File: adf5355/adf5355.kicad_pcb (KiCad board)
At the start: 2 copper layers, 48.3 x 48.3 mm, 86 parts, among them J1 REF_IN_A, J2 RF_B, J3 RF_A_P, J4 REF_IN_B, J5 RF_A_N, J6 Conn_01x02_Male, J7 Conn_01x10_Male, U1 L7806, U2 ADM7150, U3 ADM7150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

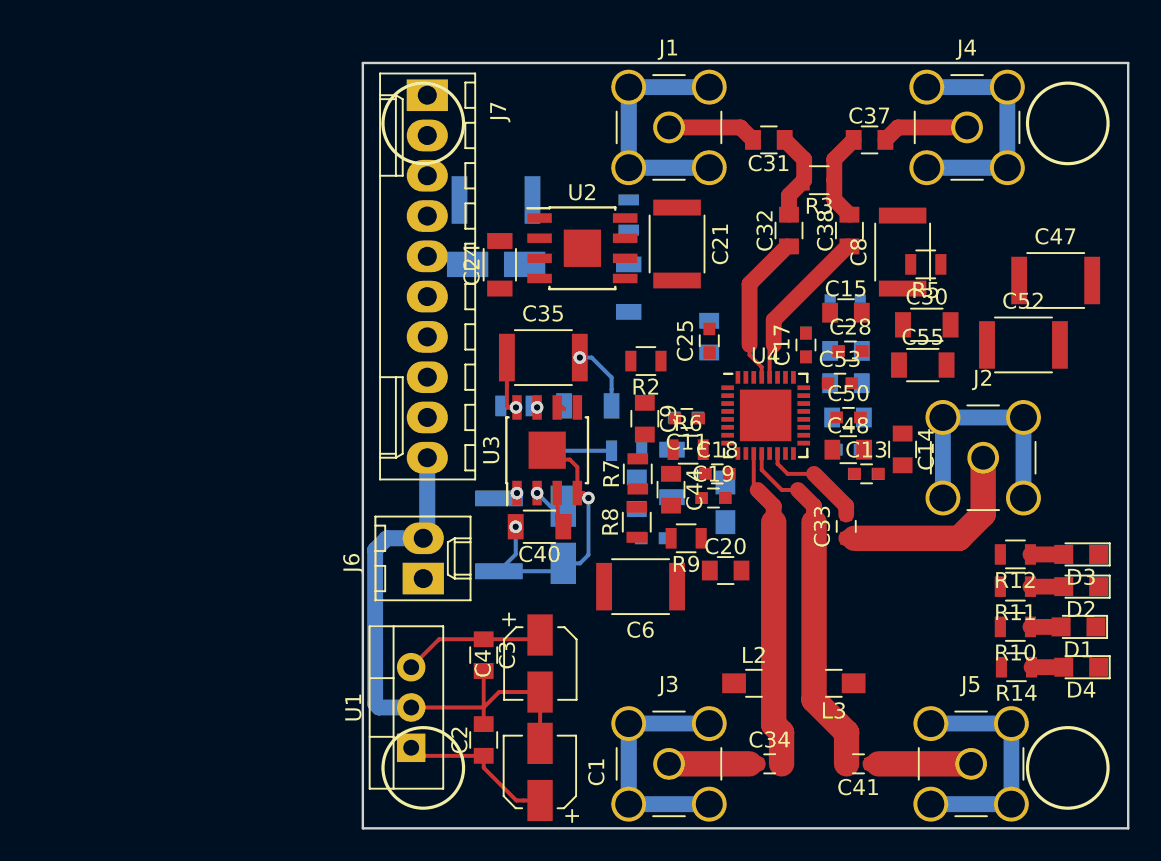
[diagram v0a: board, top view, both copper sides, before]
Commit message: Placing more components
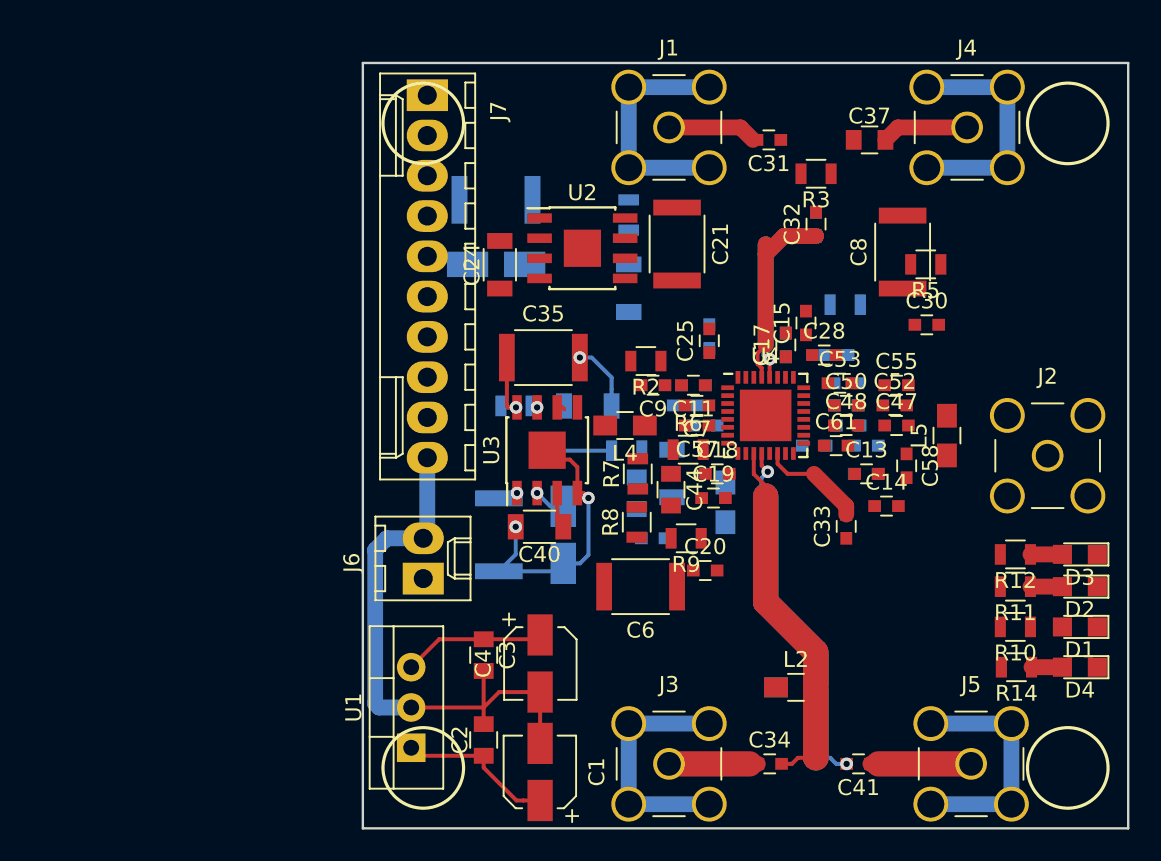
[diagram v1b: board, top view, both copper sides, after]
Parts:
- added C5: 1u, Capacitors_SMD:C_0603, B.Cu at (104.1, 100.3)
- added C56: 100p, Capacitors_SMD:C_0603, B.Cu at (105.4, 101.6)
- added C57: 10p, Capacitors_SMD:C_0603, F.Cu at (104.9, 101.6)
- added C58: 1u, Capacitors_SMD:C_0603, F.Cu at (118.1, 104.1)
- added C59: 10n, Capacitors_SMD:C_0603, B.Cu at (115.6, 102.9)
- added C60: 100p, Capacitors_SMD:C_0603, B.Cu at (112.3, 102.9)
- added C61: 10p, Capacitors_SMD:C_0603, F.Cu at (113.7, 102.9)
- added C7: 10n, Capacitors_SMD:C_0603, F.Cu at (104.9, 100.3)
- added L4: L, Capacitors_SMD:C_0805_HandSoldering, F.Cu at (100.3, 101.6)
- added L5: L, Capacitors_SMD:C_0805_HandSoldering, F.Cu at (120.7, 102.2)
- C14, C15, C20, C26, C29, C31, C32, C48, C51, C54, C9: footprint Capacitors_SMD:C_0805 -> Capacitors_SMD:C_0603
- C30, C55: footprint Capacitors_SMD:C_1206 -> Capacitors_SMD:C_0603
- C38: footprint Capacitors_SMD:C_0805 -> Capacitors_SMD:C_0603; moved to B.Cu
- C47, C52: footprint Capacitors_SMD:C_1812 -> Capacitors_SMD:C_0603
- L3: moved to B.Cu
- moved C47 13.6 mm to (117.5, 101.6)
- moved C52 8.97 mm to (117.4, 100.3)
- moved J2 4.07 mm to (127.0, 103.5)
- moved C14 3.71 mm to (116.8, 106.7), turned to 0 degrees
- moved L2 2.66 mm to (111.1, 118.1)
- moved C15 2.61 mm to (111.8, 95.1), turned to 90 degrees
- moved L3 2.41 mm to (111.1, 118.1), turned to 0 degrees
- moved C9 2.17 mm to (102.1, 99.1), turned to 180 degrees
- moved C38 2.15 mm to (112.4, 88.9)
- moved C11 2.14 mm to (104.7, 99.1)
- moved C55 2.08 mm to (117.5, 99.1)
- moved C10 2.08 mm to (104.7, 99.1)
- moved C32 1.75 mm to (112.4, 88.9)
- moved C28 1.67 mm to (112.9, 97.2)
- moved C48 1.53 mm to (114.3, 101.6)
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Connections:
- U2 pad 5: Net-(U2-Pad5) -> Net-(C23-Pad1)
- U3 pad 5: Net-(U3-Pad5) -> Net-(C39-Pad1)
- U4 pad 17: /5V -> Net-(C58-Pad1)
- U4 pad 6: /5V -> Net-(C5-Pad1)
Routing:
- net GND: track 137.1 -> 121.8 mm
- net Net-(C33-Pad1): track 12.8 -> 0.00 mm
- net Net-(C37-Pad1): track 5.62 -> 0.00 mm
- net Net-(C31-Pad1): track 5.62 -> 0.00 mm
- net Net-(C32-Pad1): track 9.68 -> 12.4 mm
- net Net-(C34-Pad2): track 20.8 -> 23.1 mm
- net Net-(D1-Pad2): track 1.93 -> 0.00 mm
- net Net-(C38-Pad1): track 10.4 -> 12.3 mm, vias 0 -> 1
- net Net-(C41-Pad2): track 22.9 -> 23.0 mm, vias 0 -> 2

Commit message: More layout placement
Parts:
- C5: moved to F.Cu
- moved C39 19.0 mm to (79.2, 97.5)
- moved C35 17.8 mm to (77.4, 97.3)
- moved C36 17.8 mm to (78.7, 108.5)
- moved C40 17.8 mm to (77.2, 108.0)
- moved R4 17.8 mm to (75.7, 100.4)
- moved U3 17.8 mm to (77.7, 103.2)
- moved C42 17.7 mm to (74.7, 108.5)
- moved R2 17.1 mm to (84.9, 101.1)
- moved C5 3.78 mm to (100.6, 101.6)
- moved C14 3.35 mm to (113.5, 106.2)
- moved C33 3.05 mm to (111.3, 108.0)
- moved C55 3.03 mm to (115.8, 96.5)
- moved L5 3.00 mm to (118.9, 104.6), turned to 0 degrees
- moved C12 2.78 mm to (112.8, 104.6)
- moved C7 2.74 mm to (102.6, 101.9), turned to 270 degrees
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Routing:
- net GND: track 121.8 -> 114.3 mm
- net Net-(C33-Pad2): track 6.62 -> 2.19 mm
- net Net-(C38-Pad1): track 12.3 -> 11.5 mm
- net Net-(C32-Pad1): track 12.4 -> 11.6 mm

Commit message: More placing
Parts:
- C43: footprint Capacitors_SMD:C_1206 -> Capacitors_SMD:C_0603; moved to F.Cu
- C44: footprint Capacitors_SMD:C_0805 -> Capacitors_SMD:C_0603
- C45: footprint Capacitors_SMD:C_0805 -> Capacitors_SMD:C_0603; moved to F.Cu
- C46: moved to F.Cu
- C47: footprint Capacitors_SMD:C_0603 -> Capacitors_SMD:C_1812
- R13: footprint Resistors_SMD:R_0805 -> Resistors_SMD:R_0603; moved to F.Cu
- R6, R7, R8, R9: footprint Resistors_SMD:R_0805 -> Resistors_SMD:R_0603
- moved C21 26.7 mm to (77.2, 86.1)
- moved U2 26.7 mm to (71.2, 86.4)
- moved C23 26.7 mm to (74.2, 88.9)
- moved C24 26.7 mm to (66.0, 87.4)
- moved R1 26.7 mm to (74.2, 84.3)
- moved C27 26.3 mm to (66.0, 84.8)
- moved C22 26.2 mm to (66.0, 91.9)
- moved C18 8.64 mm to (105.9, 114.3)
- moved R5 8.13 mm to (120.4, 99.5), turned to 90 degrees
- moved C19 5.34 mm to (106.2, 112.5)
- moved R13 5.00 mm to (105.0, 105.4), turned to 180 degrees
- moved R9 4.87 mm to (107.1, 105.3), turned to 270 degrees
- moved C30 3.57 mm to (115.8, 95.0)
- moved C46 3.48 mm to (105.4, 107.6), turned to 270 degrees
- moved C44 2.52 mm to (101.9, 104.6)
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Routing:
- net /3V3: track 0.00 -> 11.8 mm, vias 0 -> 2
- net Net-(R5-Pad1): track 0.00 -> 8.87 mm
- net Net-(R9-Pad1): track 0.00 -> 8.39 mm, vias 0 -> 1
- net Net-(C5-Pad1): track 0.00 -> 6.47 mm, vias 0 -> 1
- net Net-(C37-Pad1): track 0.00 -> 5.61 mm, vias 0 -> 1
- net Net-(C31-Pad1): track 0.00 -> 5.48 mm
- net Net-(C53-Pad1): track 0.00 -> 4.57 mm, vias 0 -> 1
- net Net-(C50-Pad1): track 0.00 -> 4.52 mm
- net GND: track 114.3 -> 116.4 mm, vias 3 -> 13
- net Net-(D1-Pad2): track 0.00 -> 2.01 mm
- net Net-(C25-Pad1): track 0.00 -> 1.65 mm, vias 0 -> 1
- net Net-(C58-Pad1): track 0.00 -> 0.81 mm
- added copper zone on B.Cu, net GND

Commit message: Started routing
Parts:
- L1: moved to F.Cu
- moved C18 4.38 mm to (106.7, 110.0), turned to 180 degrees
- moved C47 2.71 mm to (120.1, 102.1)
- moved C45 2.13 mm to (96.9, 106.8)
- moved R8 2.13 mm to (101.2, 107.6)
- moved R9 2.13 mm to (105.0, 105.9)
- moved C43 2.13 mm to (101.1, 105.3)
- moved C44 2.13 mm to (99.8, 105.3)
- moved R13 2.13 mm to (103.0, 106.0)
- moved C46 2.13 mm to (103.4, 108.2)
- moved R6 2.13 mm to (103.0, 104.6)
- moved R7 2.13 mm to (98.4, 106.9)
- moved C33 2.05 mm to (111.0, 105.9)
- moved C20 1.37 mm to (106.7, 111.3), turned to 180 degrees
- moved L1 1.27 mm to (107.4, 106.9)
- moved C19 0.51 mm to (106.7, 112.5), turned to 180 degrees
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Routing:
- net GND: track 116.4 -> 311.7 mm, vias 13 -> 50
- net Net-(C33-Pad1): track 0.00 -> 18.0 mm
- net /5V: track 2.05 -> 19.1 mm, vias 1 -> 3
- net /3V3: track 11.8 -> 22.8 mm
- net Net-(C28-Pad1): track 0.35 -> 5.65 mm, vias 0 -> 2
- net Net-(C43-Pad1): track 0.00 -> 4.72 mm
- net Net-(R6-Pad2): track 0.00 -> 4.52 mm
- net Net-(C45-Pad1): track 0.00 -> 3.69 mm
- net Net-(C46-Pad1): track 0.00 -> 3.43 mm
- net Net-(C58-Pad1): track 0.81 -> 3.82 mm, vias 0 -> 2
- net Net-(R9-Pad1): track 8.39 -> 10.0 mm, vias 1 -> 2
- net Net-(C43-Pad2): track 0.00 -> 1.16 mm
- net Net-(C50-Pad1): track 4.52 -> 5.12 mm, vias 0 -> 1
- added copper zone on In2.Cu, net /5V
- added copper zone on In1.Cu, net GND
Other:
- copper layers 2 -> 4

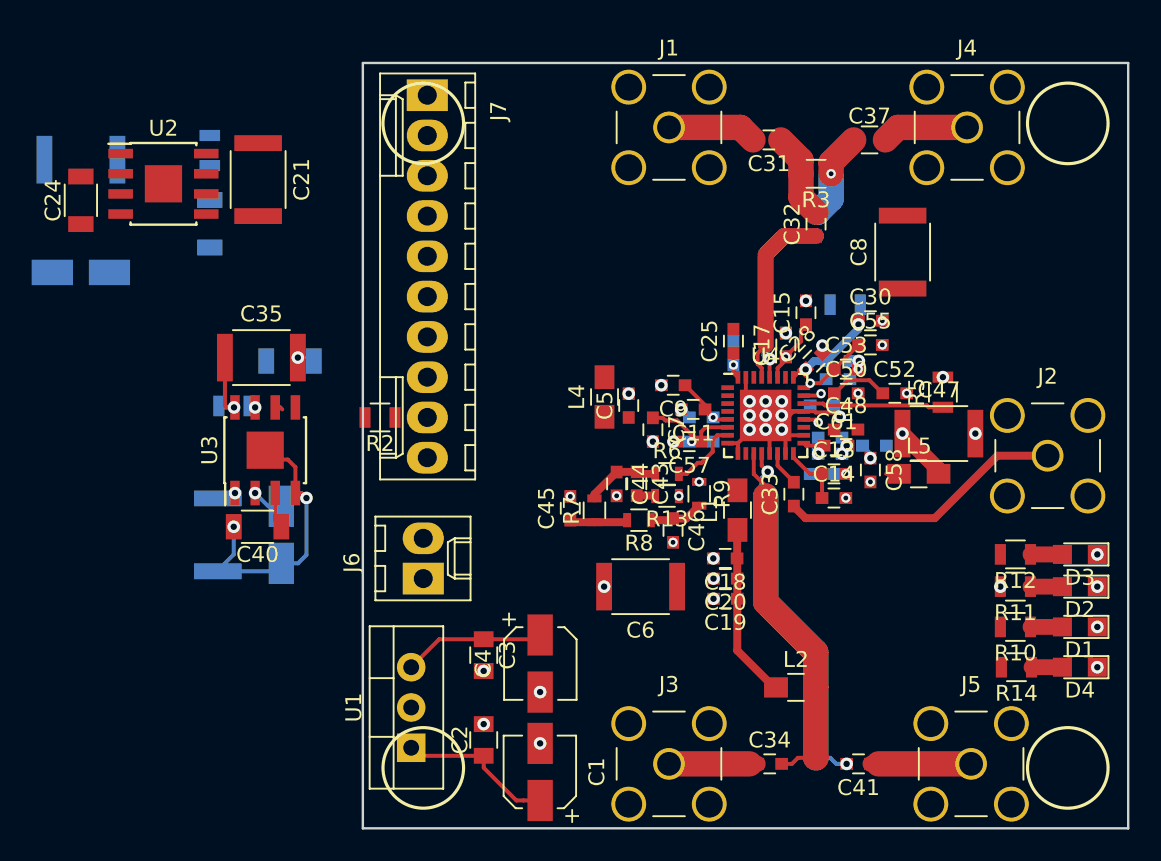
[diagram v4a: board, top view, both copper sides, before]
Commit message: Placement of LDOs and components
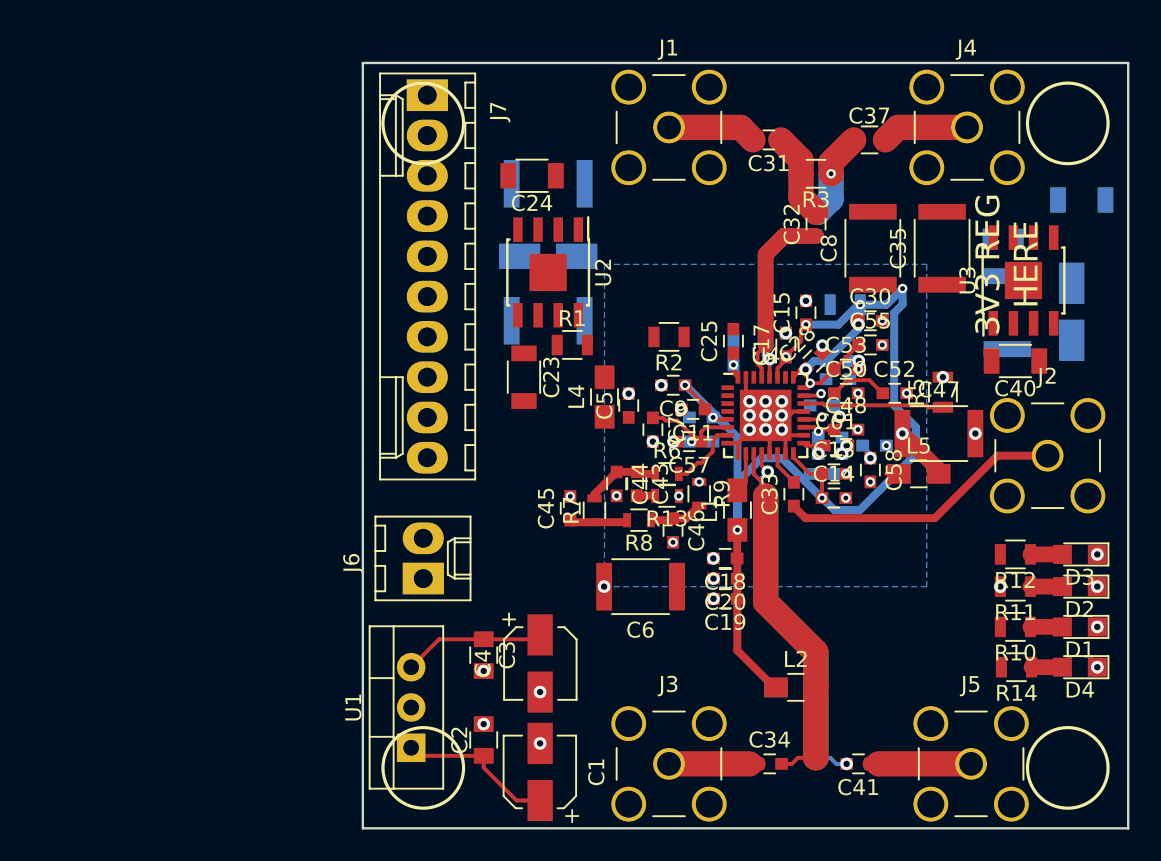
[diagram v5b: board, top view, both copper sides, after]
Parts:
- C21: moved to B.Cu
- C23, R1: moved to F.Cu
- moved C36 51.8 mm to (128.5, 94.4)
- moved C42 51.7 mm to (124.5, 94.5)
- moved C39 50.9 mm to (129.1, 87.4)
- moved R4 49.6 mm to (124.2, 89.8)
- moved U3 49.0 mm to (125.5, 92.5)
- moved C40 48.9 mm to (125.0, 97.5)
- moved C35 43.5 mm to (120.3, 90.4), turned to 90 degrees
- moved C27 29.5 mm to (95.5, 86.4)
- moved C22 29.5 mm to (95.5, 90.9)
- moved C24 28.5 mm to (94.5, 85.9), turned to 180 degrees
- moved R1 25.9 mm to (97.0, 96.5), turned to 0 degrees
- moved U2 24.9 mm to (95.5, 91.9), turned to 270 degrees
- moved C23 22.0 mm to (94.0, 98.6)
- moved C21 20.3 mm to (95.5, 95.0), turned to 180 degrees
- moved R2 18.9 mm to (103.1, 96.0)
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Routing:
- net /3V3: track 22.8 -> 69.3 mm, vias 2 -> 9
- net GND: track 311.7 -> 295.5 mm, vias 50 -> 49
- net /6V: track 13.7 -> 8.97 mm, vias 1 -> 0
- net Net-(L1-Pad2): track 0.00 -> 2.54 mm
- net Net-(C40-Pad1): track 2.28 -> 0.00 mm
- net Net-(C42-Pad1): track 1.28 -> 0.00 mm, vias 1 -> 0
- net Net-(R9-Pad1): track 10.0 -> 10.7 mm
- net Net-(R4-Pad1): track 0.42 -> 0.00 mm, vias 1 -> 0
- added copper zone on B.Cu, net /3V3
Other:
- board text added: "3V3 REG HERE"

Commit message: More layout
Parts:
- moved C22 5.72 mm to (101.2, 91.0), turned to 270 degrees
- moved C42 2.93 mm to (121.5, 94.2)
- moved C21 0.62 mm to (94.9, 95.0)
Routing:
- net GND: track 295.5 -> 361.6 mm, vias 49 -> 70
- net Net-(C24-Pad1): track 0.00 -> 4.30 mm
- net /6V: track 8.97 -> 13.2 mm, vias 0 -> 1
- net Net-(C23-Pad1): track 0.00 -> 3.83 mm
- net Net-(C27-Pad1): track 0.00 -> 3.05 mm, vias 0 -> 1
- net Net-(R1-Pad1): track 0.00 -> 1.90 mm

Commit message: More
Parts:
- moved C17 0.51 mm to (110.5, 96.0)
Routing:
- net /5V: track 19.6 -> 66.0 mm, vias 3 -> 5
- net /3V3: track 69.3 -> 114.7 mm, vias 9 -> 11
- net Net-(R15-Pad1): track 0.00 -> 6.31 mm, vias 0 -> 1
- net Net-(C58-Pad1): track 3.82 -> 8.46 mm
- net GND: track 361.6 -> 365.7 mm, vias 70 -> 63
- net Net-(C42-Pad1): track 0.00 -> 4.06 mm, vias 0 -> 1
- net Net-(C39-Pad1): track 0.00 -> 3.76 mm, vias 0 -> 1
- net Net-(R4-Pad1): track 0.00 -> 2.94 mm, vias 0 -> 1
- net Net-(C40-Pad1): track 0.00 -> 2.53 mm
- net Net-(C50-Pad1): track 5.12 -> 6.99 mm
- removed copper zone on B.Cu, net GND

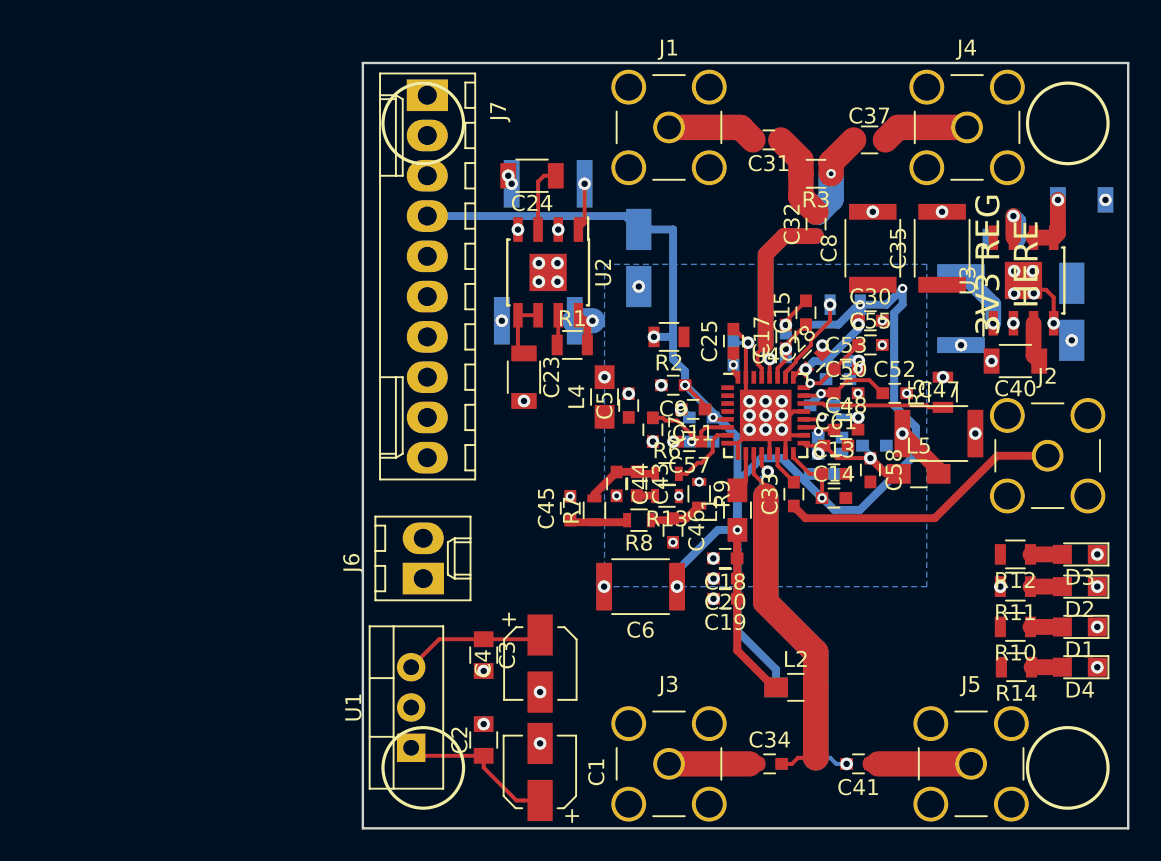
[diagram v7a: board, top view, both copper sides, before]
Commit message: Layout fully routed, now needs finilizing, moving vias to make better powerplanes, route diffpairs properly etc.
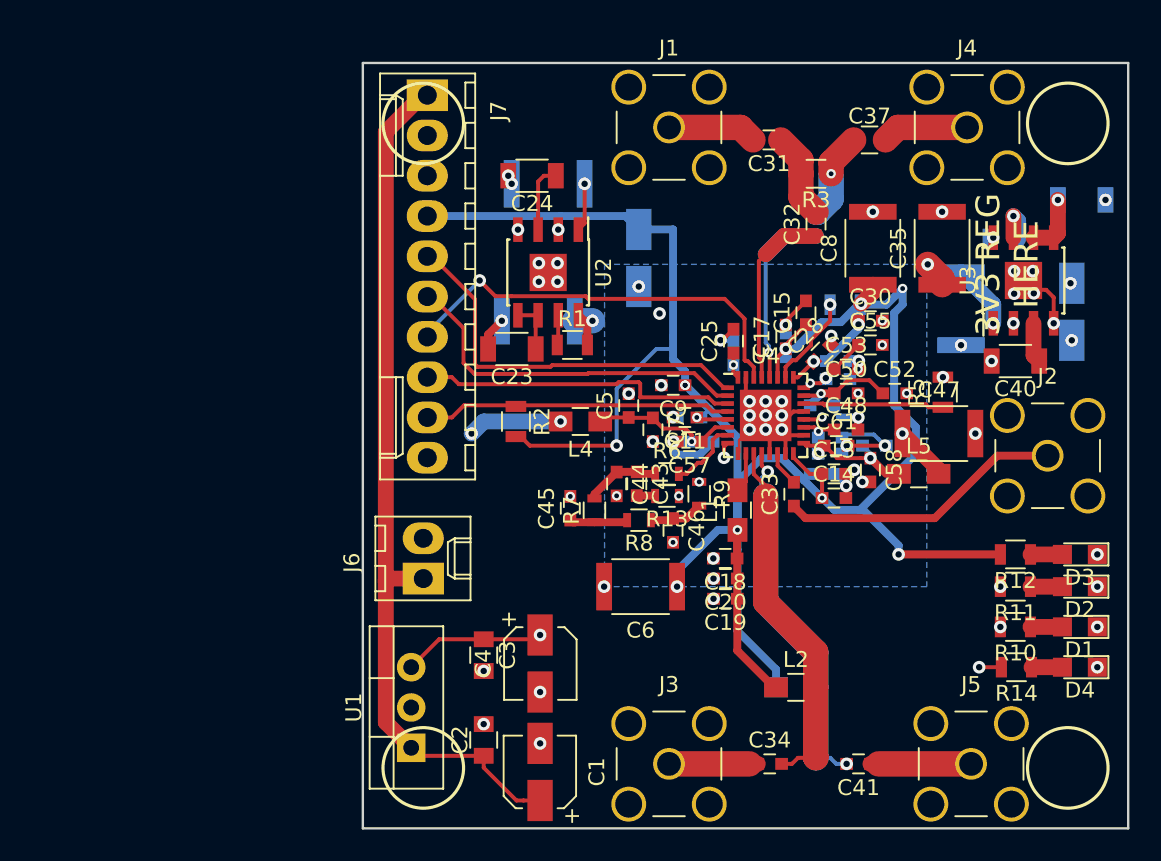
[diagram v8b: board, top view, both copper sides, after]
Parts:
- moved R2 11.0 mm to (93.5, 101.3), turned to 270 degrees
- moved L4 2.17 mm to (97.5, 101.3), turned to 180 degrees
- moved C23 1.93 mm to (93.2, 96.8), turned to 180 degrees
- moved C10 0.76 mm to (104.4, 101.1)
- moved C11 0.73 mm to (104.1, 101.1)
- moved C28 0.72 mm to (112.8, 97.0)
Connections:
- C44 pad 2: GND -> GNDA
- C45 pad 2: GND -> GNDA
- C46 pad 2: GND -> GNDA
- J7 pad 7: /LE -> /MUX
- J7 pad 8: /MUX -> /LE
- R13 pad 1: GND -> GNDA
- U4 pad 8: GND -> GNDA
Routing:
- net /6V: track 13.2 -> 117.7 mm, vias 1 -> 5
- net /MUX: track 0.00 -> 88.8 mm, vias 0 -> 2
- net /VIN: track 9.94 -> 55.6 mm
- net /5V: track 66.0 -> 99.2 mm, vias 5 -> 8
- net /3V3: track 114.7 -> 141.9 mm, vias 11 -> 12
- net /CLK: track 0.00 -> 24.9 mm
- net /DATA: track 0.00 -> 22.9 mm
- net /LE: track 0.00 -> 20.2 mm
- net /CE: track 0.00 -> 19.4 mm
- net GNDA: track 0.00 -> 15.4 mm, vias 0 -> 5
- net Net-(C5-Pad1): track 6.47 -> 9.57 mm
- net Net-(C53-Pad1): track 4.57 -> 4.65 mm, vias 1 -> 2
- added copper zone on In2.Cu, net /6V
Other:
- net class 50_ohm: clearance 0.2 -> 0.12
- net class Default: clearance 0.2 -> 0.12
- rule trace_clearance: 0.2 -> 0.12
- rule trace_min: 0.2 -> 0.12
